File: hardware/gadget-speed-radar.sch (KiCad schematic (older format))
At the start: 27 parts, among them P1 POWER, P2 LCD_I2C, P3 AMP_TO_MCU, P4 AMP_TO_RADAR, P5 RADAR, U1 LM324N, U2 Arduino Nano

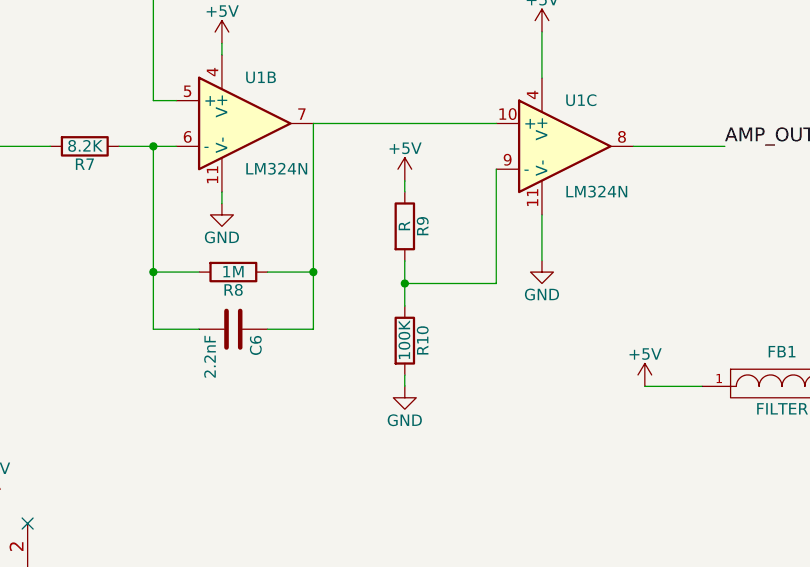
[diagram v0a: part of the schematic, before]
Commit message: tested freq averaging and range
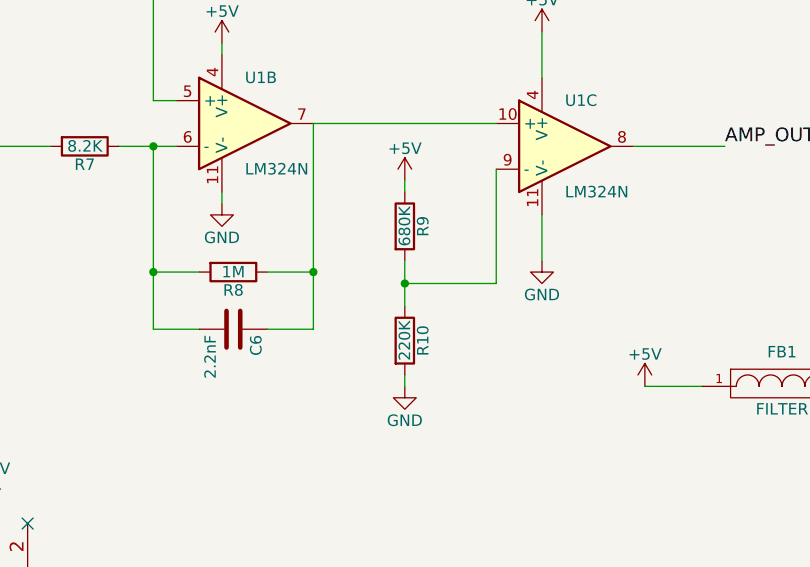
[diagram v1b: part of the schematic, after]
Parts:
- R10: value 100K -> 220K
- R9: value R -> 680K
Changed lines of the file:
@@
 LIBS:valves
 LIBS:arduino
+LIBS:gadget-speed-radar-cache
 EELAYER 25 0
 EELAYER END
@@
 P 6100 2600
 F 0 "R9" V 6180 2600 50  0000 C CNN
-F 1 "R" V 6100 2600 50  0000 C CNN
+F 1 "680K" V 6100 2600 50  0000 C CNN
 F 2 "" V 6030 2600 50  0000 C CNN
 F 3 "" H 6100 2600 50  0000 C CNN
@@
 P 6100 3100
 F 0 "R10" V 6180 3100 50  0000 C CNN
-F 1 "100K" V 6100 3100 50  0000 C CNN
+F 1 "220K" V 6100 3100 50  0000 C CNN
 F 2 "" V 6030 3100 50  0000 C CNN
 F 3 "" H 6100 3100 50  0000 C CNN
